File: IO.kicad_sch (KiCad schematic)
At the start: 47 parts, among them J1 Connector, USB-TYPE-C-16P, J2 Conn_01x02, Q3 AO3401A, Q4 AO3401A, SW1 SS-2235-H2.0, U1 TP4054, U3 TPS63001DRCR

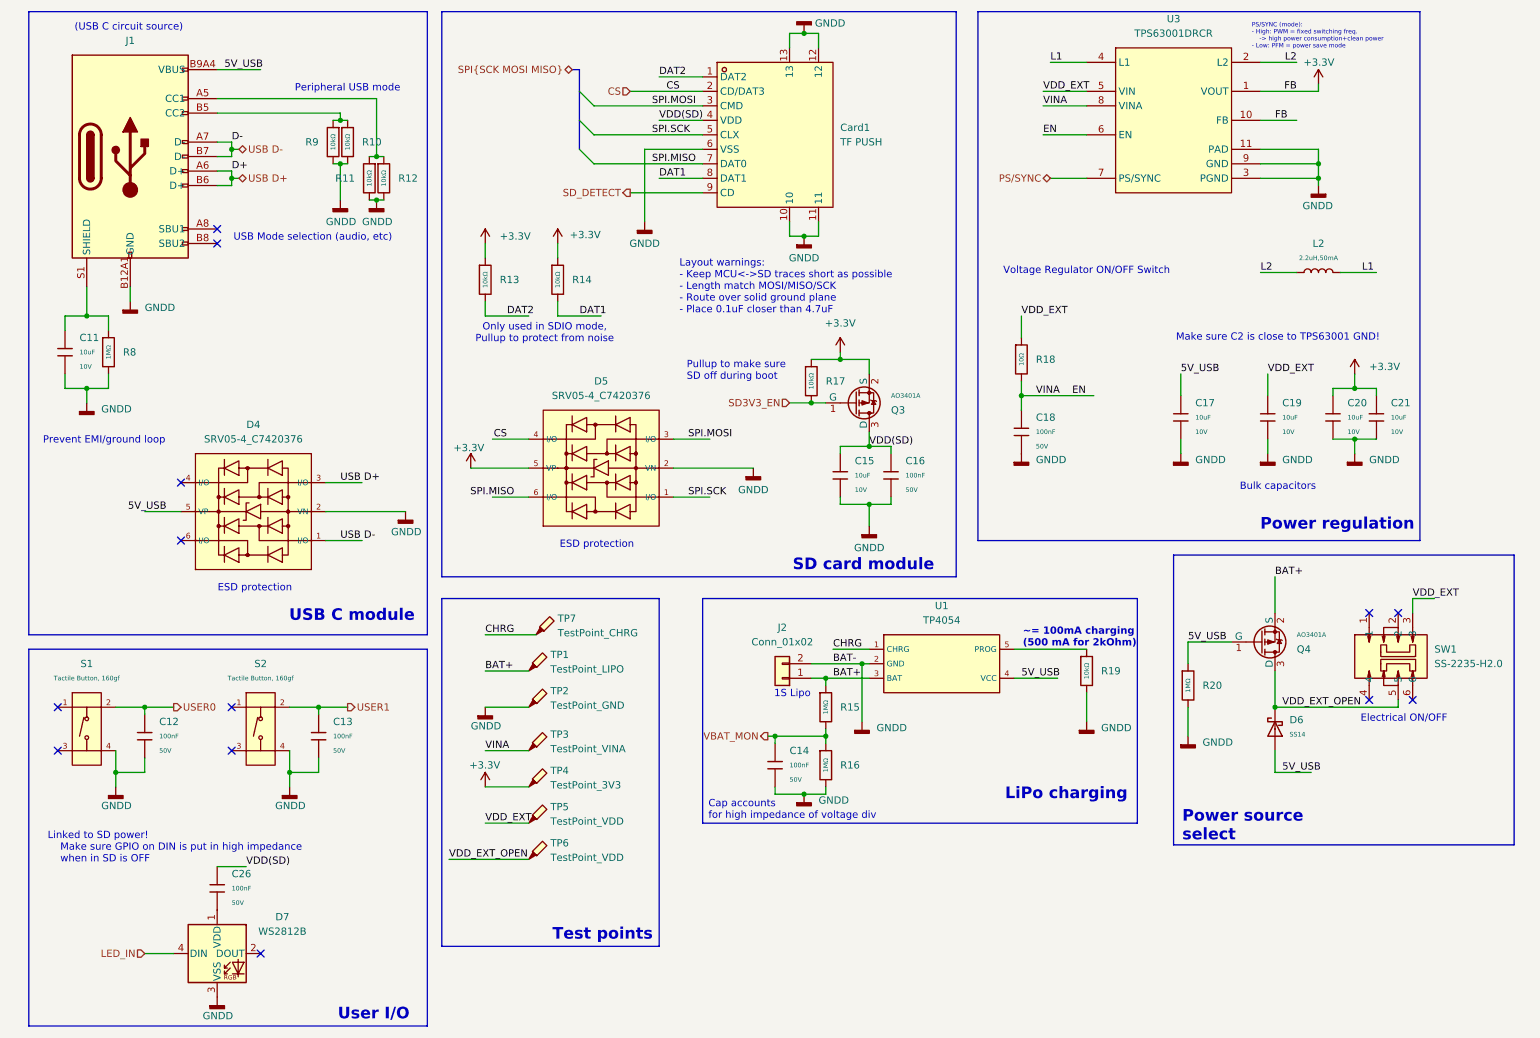
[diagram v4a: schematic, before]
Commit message: Schematic cleanup and initial layout complete
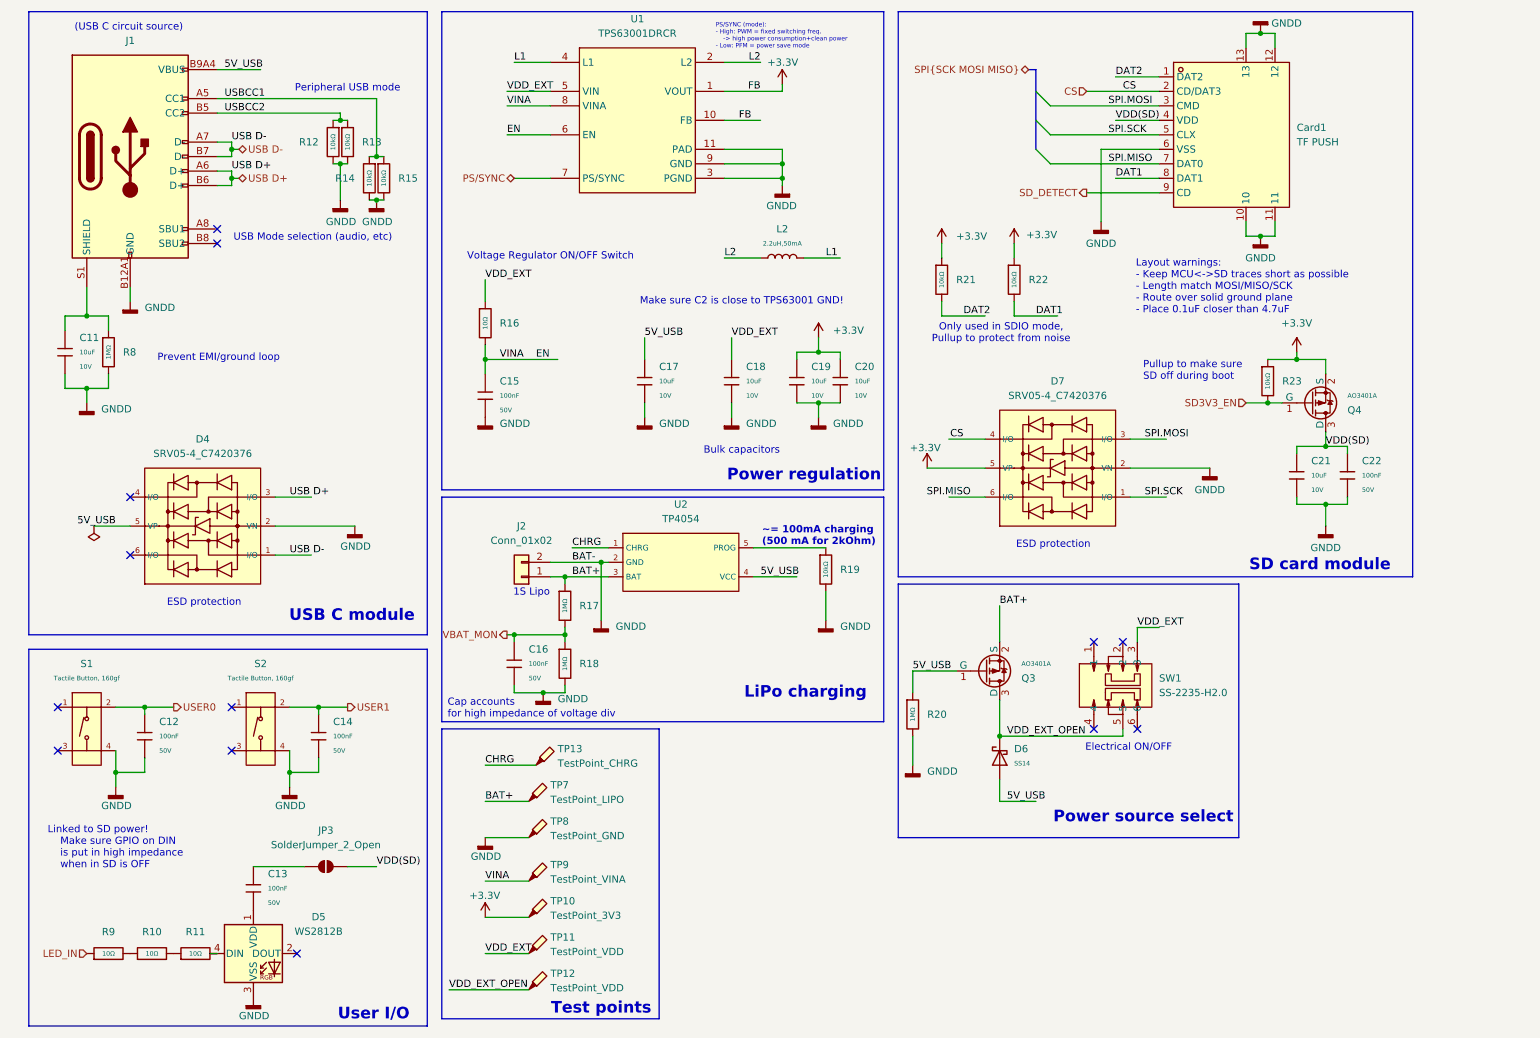
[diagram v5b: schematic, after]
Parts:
- added JP3: SolderJumper_2_Open, Jumper:SolderJumper-2_P1.3mm_Open_RoundedPad1.0x1.5mm, symbol Jumper:SolderJumper_2_Open
- added R10, R11, R9: 10Ω, PCM_JLCPCB:R_0603, symbol PCM_JLCPCB-Resistors:0603,10Ω
- C12: footprint PCM_JLCPCB:C_0603 -> PCM_JLCPCB:C_0402; symbol PCM_JLCPCB-Capacitors:0603,100nF -> PCM_JLCPCB-Capacitors:0402,100nF,(2); LCSC C14663 -> C307331; Manufacturer YAGEO -> Samsung Electro-Mechanics; Part CC0603KRX7R9BB104 -> CL05B104KB54PNC; Price 0.006USD -> 0.008USD; Stock 70324515 -> 8389599
- C13: renamed from C26; footprint PCM_JLCPCB:C_0603 -> PCM_JLCPCB:C_0402; symbol PCM_JLCPCB-Capacitors:0603,100nF -> PCM_JLCPCB-Capacitors:0402,100nF,(2); LCSC C14663 -> C307331; Manufacturer YAGEO -> Samsung Electro-Mechanics; Part CC0603KRX7R9BB104 -> CL05B104KB54PNC; Price 0.006USD -> 0.008USD; Stock 70324515 -> 8389599
- C14: renamed from C13; footprint PCM_JLCPCB:C_0603 -> PCM_JLCPCB:C_0402; symbol PCM_JLCPCB-Capacitors:0603,100nF -> PCM_JLCPCB-Capacitors:0402,100nF,(2); LCSC C14663 -> C307331; Manufacturer YAGEO -> Samsung Electro-Mechanics; Part CC0603KRX7R9BB104 -> CL05B104KB54PNC; Price 0.006USD -> 0.008USD; Stock 70324515 -> 8389599
- C15: renamed from C18; footprint PCM_JLCPCB:C_0603 -> PCM_JLCPCB:C_0402; symbol PCM_JLCPCB-Capacitors:0603,100nF -> PCM_JLCPCB-Capacitors:0402,100nF,(2); LCSC C14663 -> C307331; Manufacturer YAGEO -> Samsung Electro-Mechanics; Part CC0603KRX7R9BB104 -> CL05B104KB54PNC; Price 0.006USD -> 0.008USD; Stock 70324515 -> 8389599
- C16: renamed from C14; footprint PCM_JLCPCB:C_0603 -> PCM_JLCPCB:C_0402; symbol PCM_JLCPCB-Capacitors:0603,100nF -> PCM_JLCPCB-Capacitors:0402,100nF,(2); LCSC C14663 -> C307331; Manufacturer YAGEO -> Samsung Electro-Mechanics; Part CC0603KRX7R9BB104 -> CL05B104KB54PNC; Price 0.006USD -> 0.008USD; Stock 70324515 -> 8389599
- C22: renamed from C16; footprint PCM_JLCPCB:C_0603 -> PCM_JLCPCB:C_0402; symbol PCM_JLCPCB-Capacitors:0603,100nF -> PCM_JLCPCB-Capacitors:0402,100nF,(2); LCSC C14663 -> C307331; Manufacturer YAGEO -> Samsung Electro-Mechanics; Part CC0603KRX7R9BB104 -> CL05B104KB54PNC; Price 0.006USD -> 0.008USD; Stock 70324515 -> 8389599
- renumbered C19 to C18, C20 to C19, C21 to C20, C15 to C21, D7 to D5, D5 to D7, Q4 to Q3, Q3 to Q4, R9 to R12, R10 to R13, R11 to R14, R12 to R15, R18 to R16, R15 to R17, R16 to R18, R13 to R21, R14 to R22, R17 to R23, TP4 to TP10, TP5 to TP11, TP6 to TP12, TP7 to TP13, TP1 to TP7, TP2 to TP8, TP3 to TP9, U3 to U1, U1 to U2
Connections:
- net LED_IN: now also R9.1; no longer D5.4 (DIN)
- net VDD(SD): now also JP3.2 (B); no longer C13.1
- net USBCC1: now reaches J1.A5 (CC1), R14.1, R15.1
- net USBCC2: now reaches J1.B5 (CC2), R12.1, R13.1
- new net: R10.1, R9.2
- new net: R10.2, R11.1
- new net: D5.4 (DIN), R11.2
- new net: C13.1, JP3.1 (A)
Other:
- company: (none) -> Josef
- title: (none) -> IO
- moved on the sheet: C13, C15, C16, C17, C18, C19, C20, C21, C22, Card1, D4, D5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

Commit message: Small cleanup + linked jlcpcb parts for ordering
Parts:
- U1: footprint TPS63001DRCR:VSON-10_L3.0-W3.0-P0.50-TL-EP_TPS62410DRCR -> Libraries:VSON-10_L3.0-W3.0-P0.50-TL-EP_TPS62410DRCR
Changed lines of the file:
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@@
 			)
 		)
-		(property "Footprint" "TPS63001DRCR:VSON-10_L3.0-W3.0-P0.50-TL-EP_TPS62410DRCR"
+		(property "Footprint" "Libraries:VSON-10_L3.0-W3.0-P0.50-TL-EP_TPS62410DRCR"
 			(at 123.19 54.61 0)
 			(effects

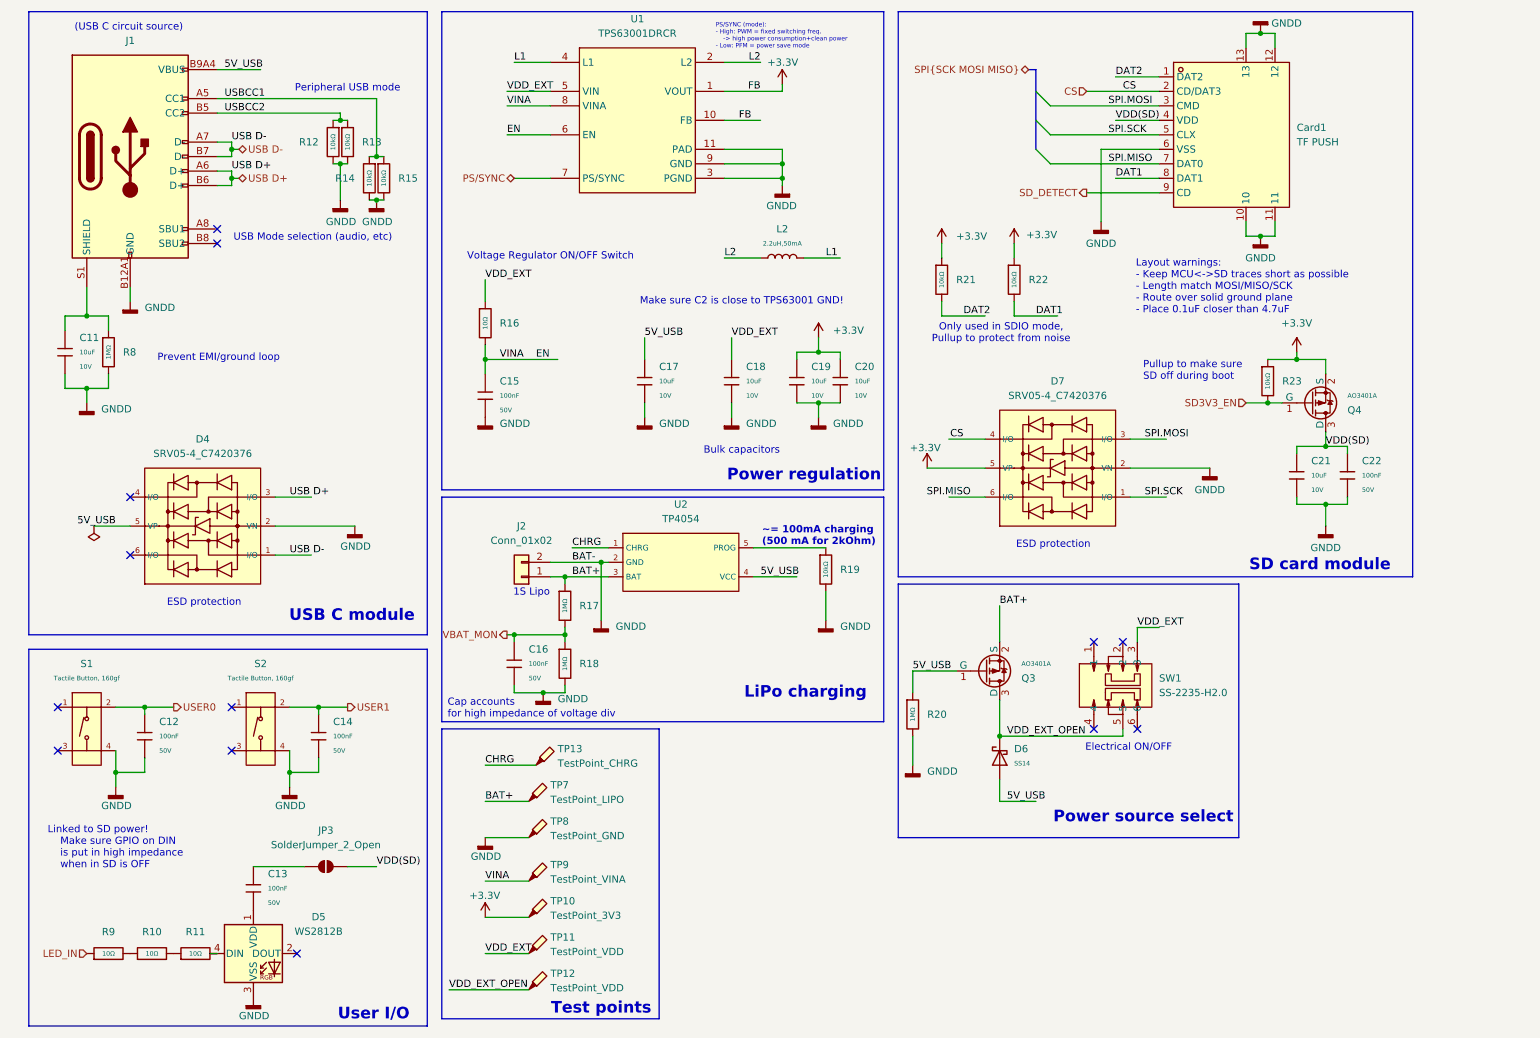
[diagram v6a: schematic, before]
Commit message: Changed some parts for more common ones
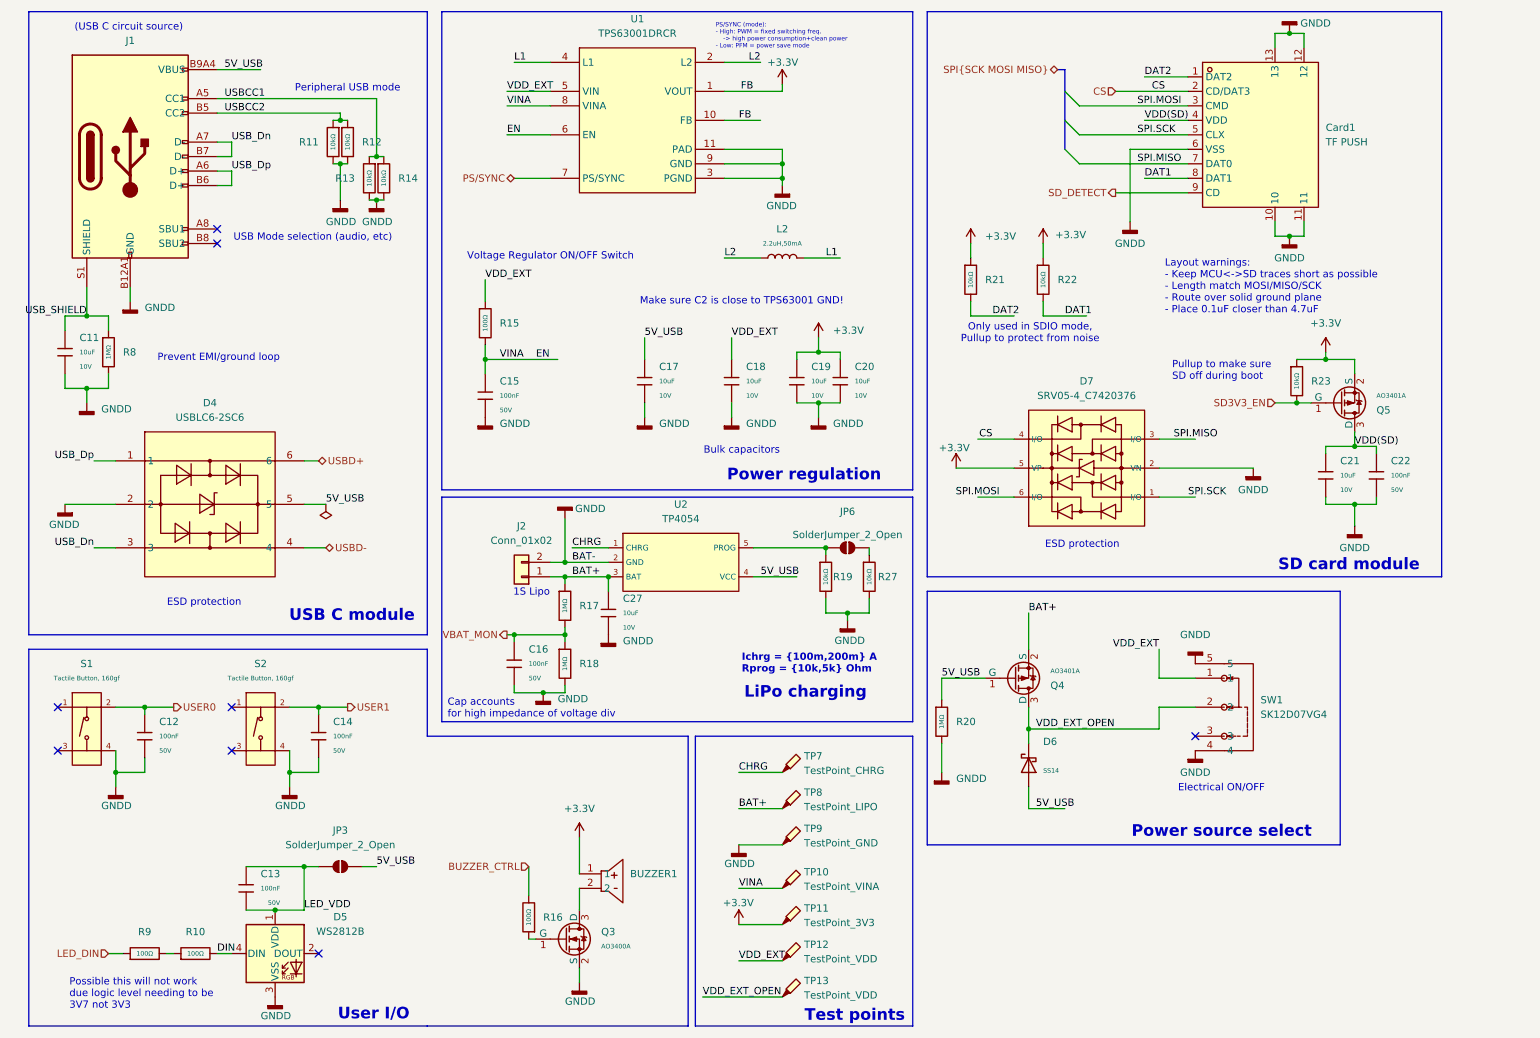
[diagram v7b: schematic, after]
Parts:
- removed D4: SRV05-4_C7420376, PCM_JLCPCB:SOT-23-6_L2.9-W1.6-P0.95-LS2.8-BL-1, symbol PCM_JLCPCB-Diode-Packages:Package, SRV05-4_C7420376
- removed R10, R11, R16, R9: 10Ω, PCM_JLCPCB:R_0603, symbol PCM_JLCPCB-Resistors:0603,10Ω
- removed SW1: SS-2235-H2.0, Libraries:SW-TH_6P-L9.0-W3.6-P2.50_SS-2235-H2.0, symbol E-paper-library:SS-2235-H2.0
- added BUZZER1: YS-MBZ9042C03R16, Libraries:BUZ-TH_BD9.0-P4.00-D0.6-FD, symbol E-paper-library:YS-MBZ9042C03R16
- added C27: 10uF, PCM_JLCPCB:C_0603, symbol PCM_JLCPCB-Capacitors:0603,10uF
- added D4: USBLC6-2SC6, Libraries:SOT-23-6_L2.9-W1.6-P0.95-LS2.8-BL, symbol E-paper-library:USBLC6-2SC6
- added JP6: SolderJumper_2_Open, Jumper:SolderJumper-2_P1.3mm_Open_RoundedPad1.0x1.5mm, symbol Jumper:SolderJumper_2_Open
- added Q3: AO3400A, PCM_JLCPCB:Q_SOT-23, symbol PCM_JLCPCB-Transistors:NMOS,AO3400A
- added R10, R15, R16, R9: 100Ω, PCM_JLCPCB:R_0603, symbol PCM_JLCPCB-Resistors:0603,100Ω
- added R27: 10kΩ, PCM_JLCPCB:R_0402, symbol PCM_JLCPCB-Resistors:0402,10kΩ
- added SW1: SK12D07VG4, Libraries:SW-TH_SK12D07VG4, symbol E-paper-library:SK12D07VG4
- renumbered Q3 to Q4, Q4 to Q5, R12 to R11, R13 to R12, R14 to R13, R15 to R14, TP9 to TP10, TP10 to TP11, TP11 to TP12, TP12 to TP13, TP13 to TP7, TP7 to TP8, TP8 to TP9
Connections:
- net +3.3V: now also U1.1 (VOUT), BUZZER1.1
- net 5V_USB: now also JP3.2 (B), D4.5
- net BAT+: now also C27.1
- net EN: now also R15.2
- net GNDD: now also C27.2, D4.2, Q3.2 (S), R27.2, SW1.4, SW1.5
- net SPI.MISO: now also D7.3 (I/O); no longer D7.6 (I/O)
- net SPI.MOSI: now also D7.6 (I/O); no longer D7.3 (I/O)
- net VDD(SD): no longer JP3.2 (B)
- net VDD_EXT: now also R15.1, SW1.1
- net VDD_EXT_OPEN: now also SW1.2
- net at R19.1, U2.5 (PROG): now also JP6.1 (A)
- net LED_VDD: now reaches C13.2, D5.1 (VDD)
- net LED_VDD: now also C13.1, JP3.1 (A)
- net DIN: now reaches D5.4 (DIN)
- net DIN: now also R10.2
- net USB_SHIELD: now reaches C11.1, J1.S1 (SHIELD), R8.1
- net USB D+ renamed USB_Dp
- net USB_Dp: now also D4.1
- net USB D- renamed USB_Dn
- net USB_Dn: now also D4.3
- new net: JP6.2 (B), R27.1
- new net: Q3.1 (G), R16.1
- new net: BUZZER1.2, Q3.3 (D)
- new net: R10.1, R9.2
- new net BUZZER_CTRL: R16.2
- new net LED_DIN: R9.1
- new net USBD+: D4.6
- new net USBD-: D4.4
- no-connect marks 13 -> 8
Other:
- note added: "Ichrg = {100m,200m} A Rprog = {10k,5k} Ohm"
- note added: "Possible this will not work due logic level needing to be 3V7 not 3V3"
- note removed: "Linked to SD power! Make sure GPIO on DIN is put in high impedance when in SD is OFF"
- note removed: "~= 100mA charging (500 mA for 2kOhm)"
- moved on the sheet: C13, C21, C22, Card1, D5, D6, D7, JP3, Q4, Q5, R19, R20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

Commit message: Finished USB, SD card and Power Mmt layout
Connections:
- net PROG: now reaches JP6.1 (A), R19.1, U2.5 (PROG)
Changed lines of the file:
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@@
+	(wire
+		(pts
+			(xy 143.51 111.76) (xy 156.21 111.76)
+		)
+		(stroke
+			(width 0)
+			(type default)
+		)
+	)
 	(wire
 		(pts
@@
 		(pts
 			(xy 151.13 86.36) (xy 154.94 86.36)
-		)
-		(stroke
-			(width 0)
-			(type default)
-		)
-	)
-	(wire
-		(pts
-			(xy 156.21 111.76) (xy 143.51 111.76)
 		)
 		(stroke
@@
 		(effects
 			(font
+				(size 1.27 1.27)
+			)
+			(justify left bottom)
+		)
+	)
+	(label "PROG"
+		(at 144.78 111.76 0)
+		(effects
+			(font
